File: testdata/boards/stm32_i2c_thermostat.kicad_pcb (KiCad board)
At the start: 2 parts, among them U1 STM32F103C8T6

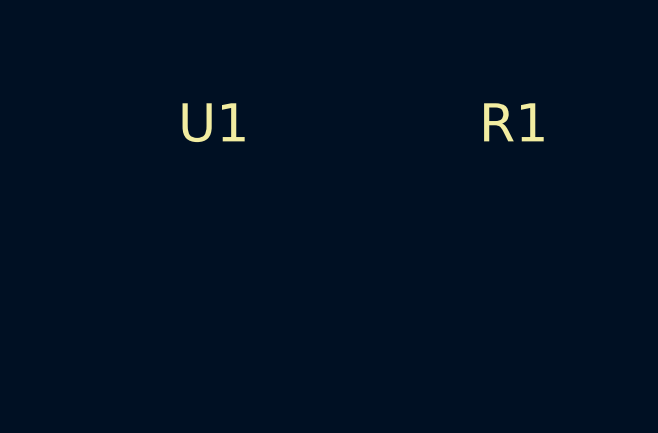
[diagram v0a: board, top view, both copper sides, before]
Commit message: Route the STM32 I2C thermostat fixture so its LM75 co-sim examples pass the static gate
The renode LM75 examples run this board through the as-built static check,
which refuses an unrouted board. The fixture now has real pad sizes (0.6 mm
SMD on its 1 mm grid, 1.6 mm THT) and copper for GND, +3V3 and FLAG, and
hauksbee check reports it clean with no shorts or clearance violations.

Signed-off-by: ETM-Code <158038827+ETM-Code@users.noreply.github.com>
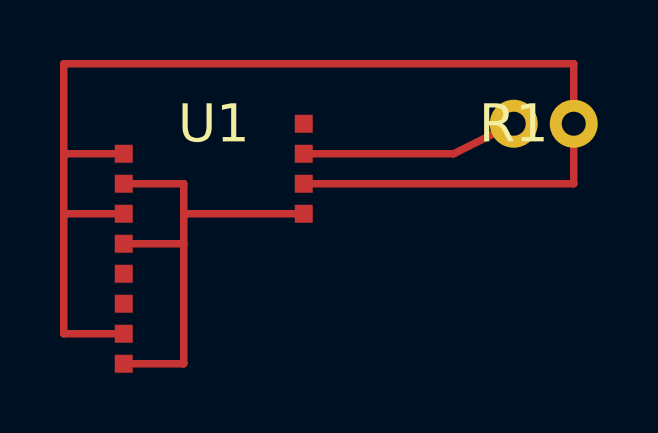
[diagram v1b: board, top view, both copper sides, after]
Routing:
- net GND: track 0.00 -> 45.0 mm
- net +3V3: track 0.00 -> 16.0 mm
- net FLAG: track 0.00 -> 7.24 mm
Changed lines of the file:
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@@
     (fp_text reference U1 (at 0 0) (layer F.SilkS))
     (fp_text value STM32F103C8T6 (at 0 2) (layer F.Fab))
-    (pad 8  smd rect (at -3 1) (net 1 "GND"))
-    (pad 9  smd rect (at -3 2) (net 2 "+3V3"))
-    (pad 15 smd rect (at 3 0) (net 6 "PA5_OUT"))
-    (pad 29 smd rect (at 3 1) (net 3 "FLAG"))
-    (pad 23 smd rect (at 3 2) (net 1 "GND"))
-    (pad 24 smd rect (at 3 3) (net 2 "+3V3"))
-    (pad 35 smd rect (at -3 3) (net 1 "GND"))
-    (pad 36 smd rect (at -3 4) (net 2 "+3V3"))
-    (pad 37 smd rect (at -3 5) (net 5 "SCL"))
-    (pad 38 smd rect (at -3 6) (net 4 "SDA"))
-    (pad 44 smd rect (at -3 7) (net 1 "GND"))
-    (pad 48 smd rect (at -3 8) (net 2 "+3V3"))
+    (pad 8  smd rect (at -3 1) (size 0.6 0.6) (layers F.Cu F.Paste F.Mask) (net 1 "GND"))
+    (pad 9  smd rect (at -3 2) (size 0.6 0.6) (layers F.Cu F.Paste F.Mask) (net 2 "+3V3"))
+    (pad 15 smd rect (at 3 0) (size 0.6 0.6) (layers F.Cu F.Paste F.Mask) (net 6 "PA5_OUT"))
+    (pad 29 smd rect (at 3 1) (size 0.6 0.6) (layers F.Cu F.Paste F.Mask) (net 3 "FLAG"))
+    (pad 23 smd rect (at 3 2) (size 0.6 0.6) (layers F.Cu F.Paste F.Mask) (net 1 "GND"))
+    (pad 24 smd rect (at 3 3) (size 0.6 0.6) (layers F.Cu F.Paste F.Mask) (net 2 "+3V3"))
+    (pad 35 smd rect (at -3 3) (size 0.6 0.6) (layers F.Cu F.Paste F.Mask) (net 1 "GND"))
+    (pad 36 smd rect (at -3 4) (size 0.6 0.6) (layers F.Cu F.Paste F.Mask) (net 2 "+3V3"))
+    (pad 37 smd rect (at -3 5) (size 0.6 0.6) (layers F.Cu F.Paste F.Mask) (net 5 "SCL"))
+    (pad 38 smd rect (at -3 6) (size 0.6 0.6) (layers F.Cu F.Paste F.Mask) (net 4 "SDA"))
+    (pad 44 smd rect (at -3 7) (size 0.6 0.6) (layers F.Cu F.Paste F.Mask) (net 1 "GND"))
+    (pad 48 smd rect (at -3 8) (size 0.6 0.6) (layers F.Cu F.Paste F.Mask) (net 2 "+3V3"))
   )
   (module Resistor_THT:R_Axial_DIN0207_L6.3mm_D2.5mm (layer F.Cu)
@@
     (fp_text reference R1 (at 0 0) (layer F.SilkS))
     (fp_text value 4k7 (at 0 2) (layer F.Fab))
-    (pad 1 thru_hole circle (at 0 0) (net 3 "FLAG"))
-    (pad 2 thru_hole circle (at 2 0) (net 1 "GND"))
+    (pad 1 thru_hole circle (at 0 0) (size 1.6 1.6) (drill 0.8) (layers *.Cu *.Mask) (net 3 "FLAG"))
+    (pad 2 thru_hole circle (at 2 0) (size 1.6 1.6) (drill 0.8) (layers *.Cu *.Mask) (net 1 "GND"))
   )
+  (segment (start 97 101) (end 95 101) (width 0.25) (layer F.Cu) (net 1))
+  (segment (start 97 103) (end 95 103) (width 0.25) (layer F.Cu) (net 1))
+  (segment (start 97 107) (end 95 107) (width 0.25) (layer F.Cu) (net 1))
+  (segment (start 95 107) (end 95 98) (width 0.25) (layer F.Cu) (net 1))
+  (segment (start 95 98) (end 112 98) (width 0.25) (layer F.Cu) (net 1))
+  (segment (start 112 98) (end 112 100) (width 0.25) (layer F.Cu) (net 1))
+  (segment (start 103 102) (end 112 102) (width 0.25) (layer F.Cu) (net 1))
+  (segment (start 112 102) (end 112 100) (width 0.25) (layer F.Cu) (net 1))
+  (segment (start 97 102) (end 99 102) (width 0.25) (layer F.Cu) (net 2))
+  (segment (start 97 104) (end 99 104) (width 0.25) (layer F.Cu) (net 2))
+  (segment (start 97 108) (end 99 108) (width 0.25) (layer F.Cu) (net 2))
+  (segment (start 99 102) (end 99 108) (width 0.25) (layer F.Cu) (net 2))
+  (segment (start 99 103) (end 103 103) (width 0.25) (layer F.Cu) (net 2))
+  (segment (start 103 101) (end 108 101) (width 0.25) (layer F.Cu) (net 3))
+  (segment (start 108 101) (end 110 100) (width 0.25) (layer F.Cu) (net 3))
 )
